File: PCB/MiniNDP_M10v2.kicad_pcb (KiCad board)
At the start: 2 copper layers, 56 x 31 mm, 22 parts, among them J1 Conn_02x20_Odd_Even, U1 AS6C8008_TSOPII, U2 HC238, U3 HC4040, U4 ABT841

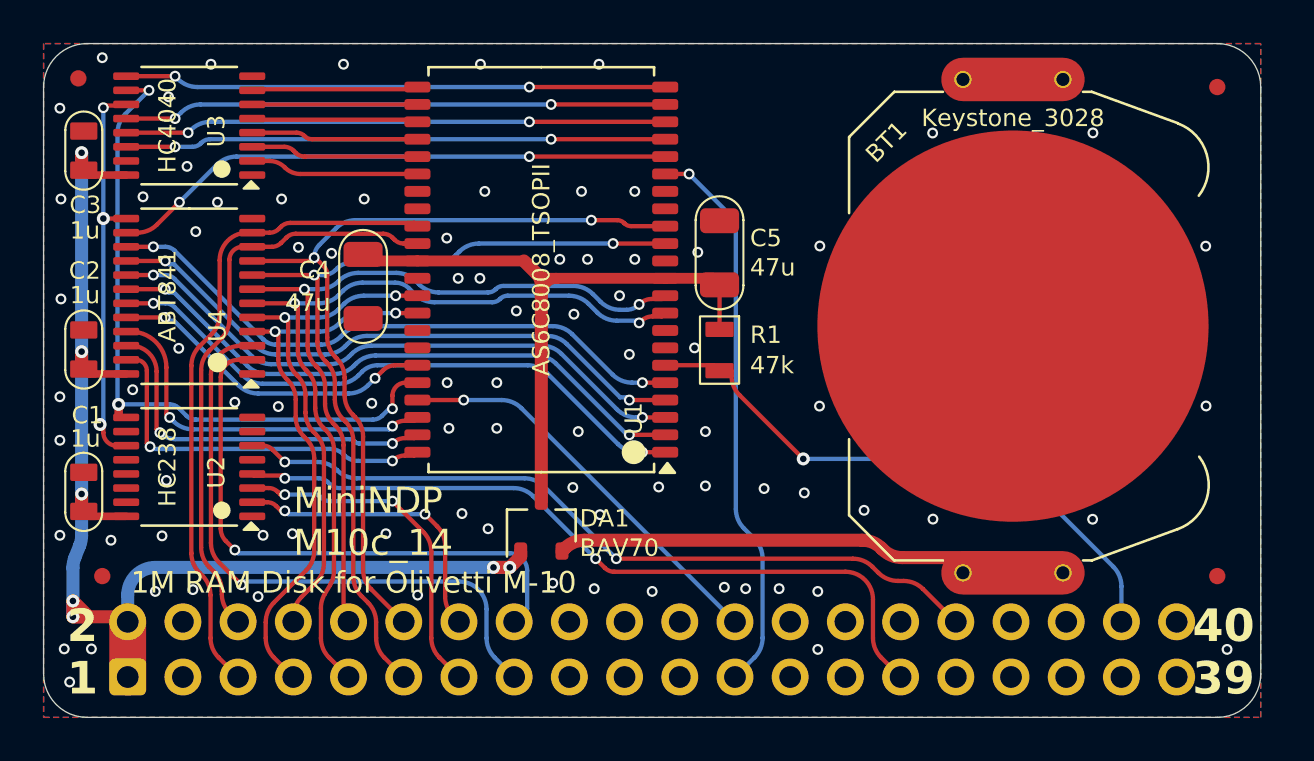
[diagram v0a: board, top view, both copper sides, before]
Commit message: Olivetti M-10 take 3. T512 pics readme.
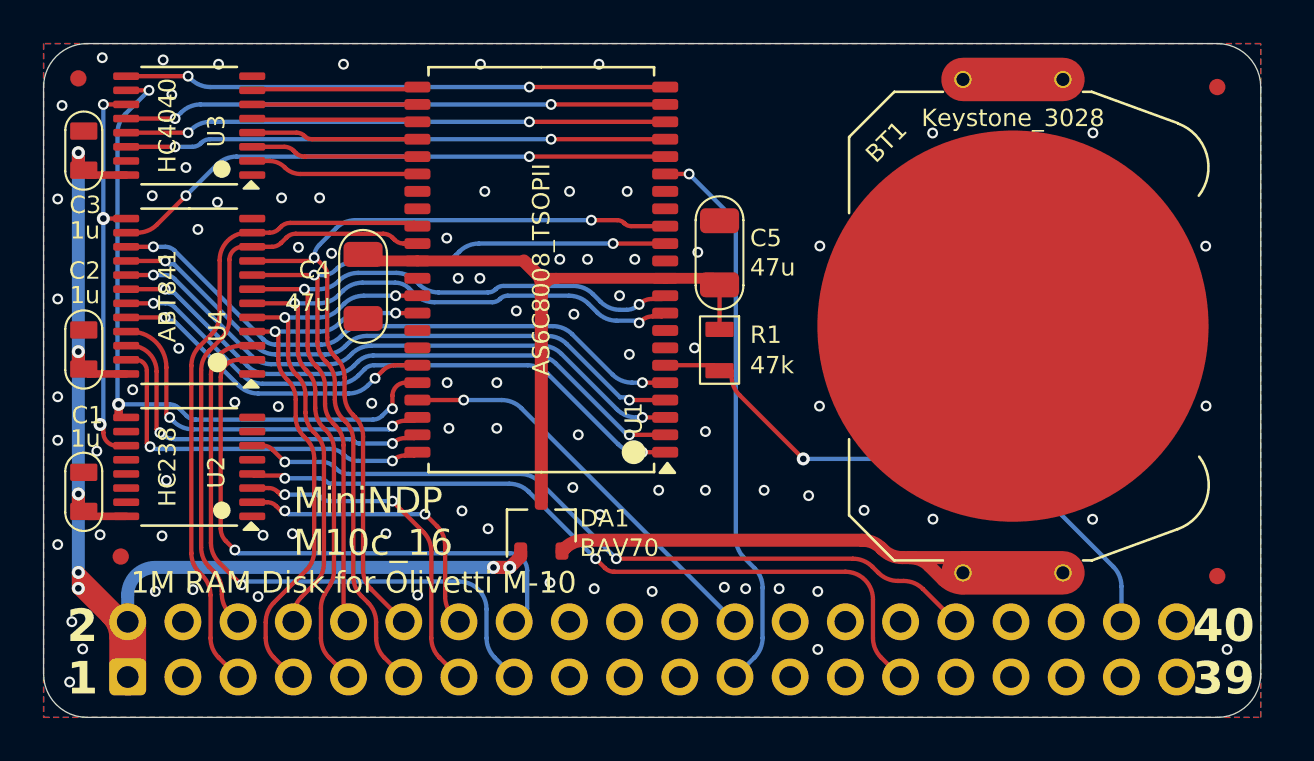
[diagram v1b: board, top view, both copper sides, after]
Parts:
- moved F3 1.24 mm to (126.9, 110.6)
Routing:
- net +BATT: track 21.4 -> 24.3 mm
- net VBUS: track 58.9 -> 61.6 mm
- net GND: vias 85 -> 87
